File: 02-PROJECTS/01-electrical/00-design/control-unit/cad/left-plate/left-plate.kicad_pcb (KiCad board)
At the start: 2 copper layers, 100 x 56 mm, 22 parts, among them J1 plate cable header 2x6 shroud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, SW1 key - hatch, SW2 key - fuel door, U1 IS31FL3218-QFLS2-TR

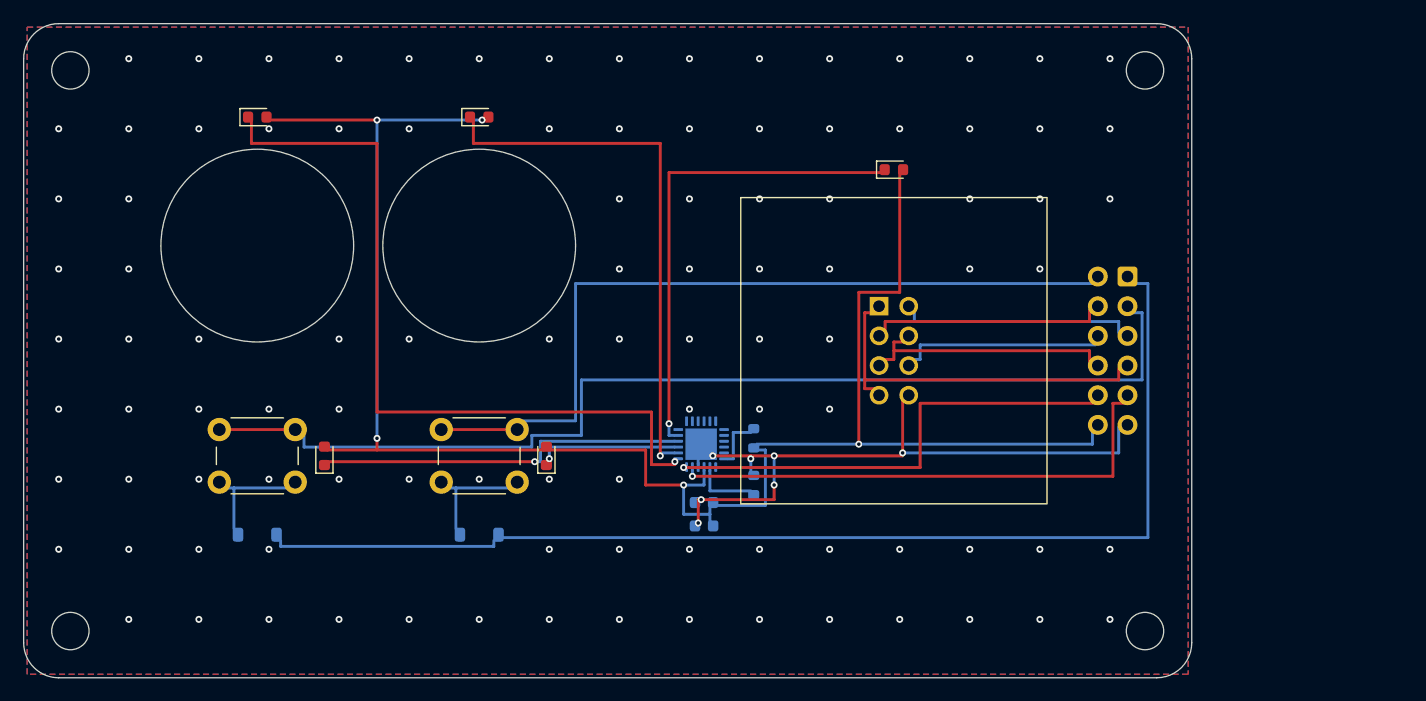
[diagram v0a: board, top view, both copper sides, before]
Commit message: Electrical: the left plate regenerated - P204 winks on the board at 19 mm, the wink lead on J2, the wink check in check.py (D-499, D-504)
Y22 done. ERC 0, DRC 0/0/0, check.py 29 checks 0 mismatches on the plate with check_winks (J2 against the L3-S1 rows that land on it, resistor values from cavity 11); the other boards unchanged. P204's footprint, J2's housing and run and R3/R4's part numbers confirm. The design README's plate row follows in the next commit with the export section.

Co-Authored-By: Claude Fable 5.1 <noreply@anthropic.com>
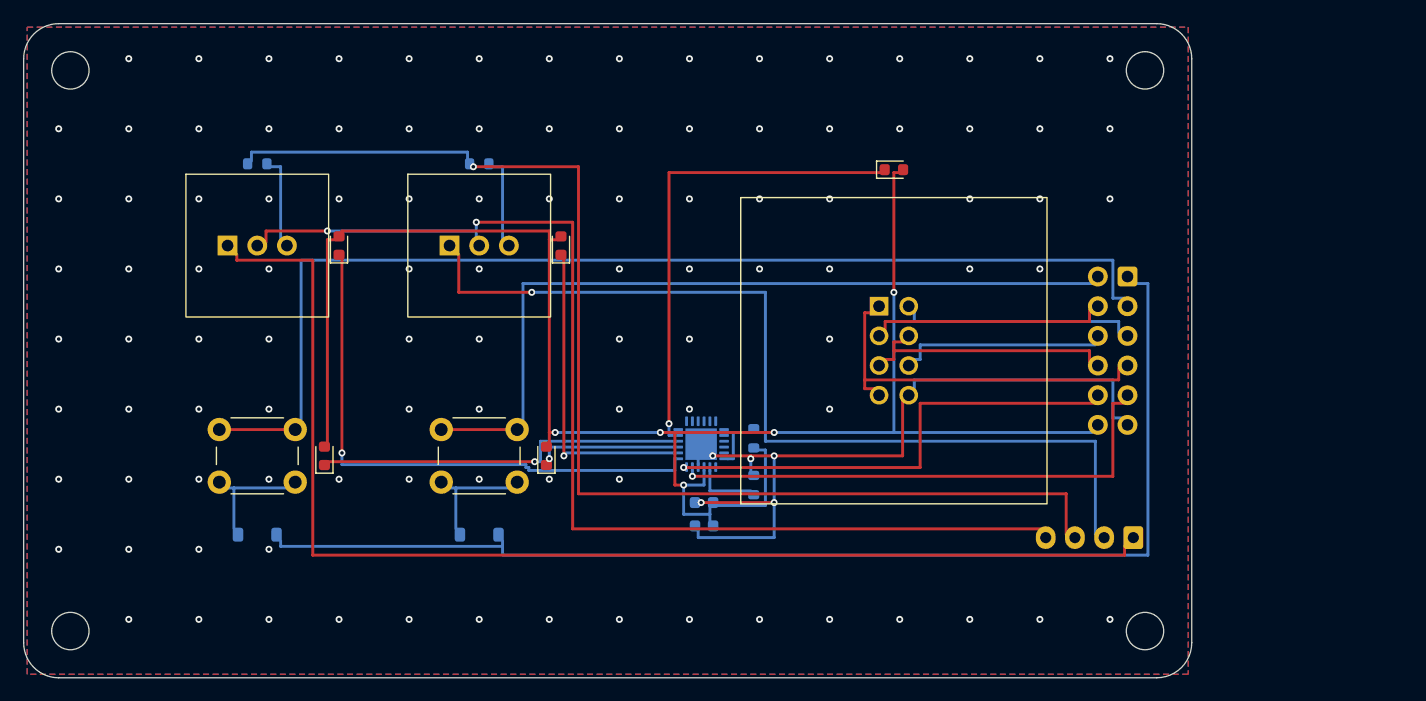
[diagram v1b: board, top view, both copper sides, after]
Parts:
- removed H5: wink L (P083) - clearance, no nets, left-plate:WinkSwitch_P083_Clearance_D16.5
- removed H6: wink R (P083) - clearance, no nets, left-plate:WinkSwitch_P083_Clearance_D16.5
- added J2: wink lead header 1x4 (L3-S1 9 / 10 / 11, commons), Connector_JST:JST_XH_B4B-XH-A_1x04_P2.50mm_Vertical, B.Cu at (95.0, 44.0)
- added R3: 18k, Resistor_SMD:R_0603_1608Metric, B.Cu at (20.0, 12.0)
- added R4: 33k, Resistor_SMD:R_0603_1608Metric, B.Cu at (39.0, 12.0)
- added SW3: wink - left (P204), left-plate:WinkSwitch_P204_SPDT_Placeholder, F.Cu at (20.0, 19.0)
- added SW4: wink - right (P204), left-plate:WinkSwitch_P204_SPDT_Placeholder, F.Cu at (39.0, 19.0)
- moved LED1 13.0 mm to (27.0, 19.0), turned to 90 degrees
- moved LED2 13.0 mm to (46.0, 19.0), turned to 90 degrees
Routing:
- net /WINK_L_NC: track 0.00 -> 102.5 mm
- net /WINK_REQ: track 0.00 -> 102.2 mm, vias 0 -> 1
- net /WINK_COM: track 0.00 -> 95.0 mm, vias 0 -> 2
- net /WINK_R_NC: track 0.00 -> 78.5 mm, vias 0 -> 1
- net /LED_WINK_R: track 46.2 -> 26.8 mm
- net /LED_WINK_L: track 66.2 -> 47.8 mm
- net GND: track 56.2 -> 65.5 mm
- net /WINK_R_NO: track 0.00 -> 7.25 mm
- net /WINK_L_NO: track 0.00 -> 7.25 mm
- net /+5V_PNL: track 155.2 -> 148.8 mm
- net /ROW1: track 97.2 -> 100.2 mm
- net /COL3: track 90.0 -> 92.5 mm
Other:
- board text added: "D-492 D-499 - provisional, confirm"
- board text added: "LEFT PLATE Y22 rev 0.02"
- board text removed: "D-492 - provisional, confirm"
- board text removed: "LEFT PLATE Y21 rev 0.01"

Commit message: Electrical: the CUR board takes the latching hazard button and the screen knob's header; its mock-up the knob (D-586, D-589, D-581)
Y62, Y50, Y51 (the CUR part). The plate board rev 0.03 from its generator: SW5 latching button with
R5 4.7 k and R6 47 k on a 5-way J2, LED6 the red triangle on OUT6 (the mirror symbol to OUT13, the
DCU's lights.h follows), J4 a STEMMA QT header for the knob's I2C board, the plate 118 x 56 (its
face's layout is block 01.60). ERC 0, DRC 0 with parity, check.py left-plate 31 / 0 with a new hazard
rule. The board script finishes leftovers with freerouting. The CUR mock-up's hazard opening and the
screen knob (24 / 24). The Digi-Key cart gains P219's board and lead.

Co-Authored-By: Claude Opus 5.5 <noreply@anthropic.com>
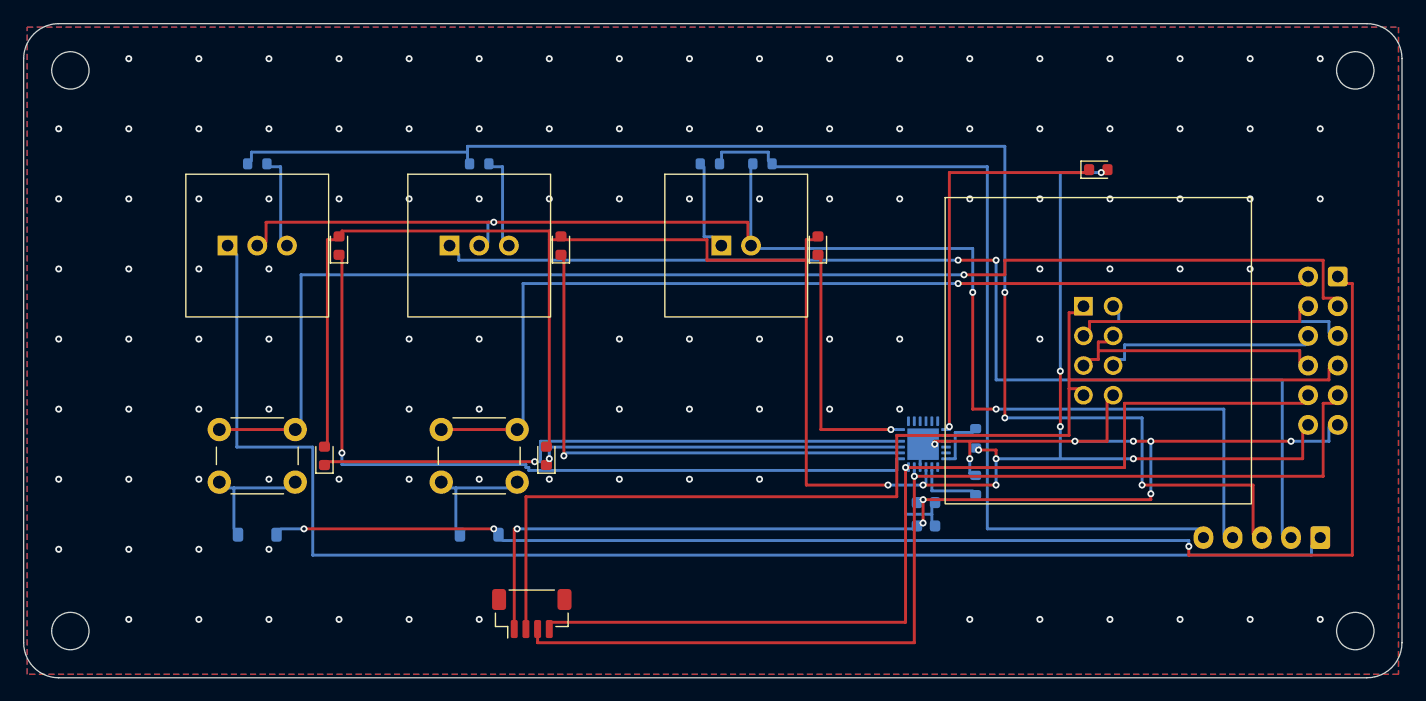
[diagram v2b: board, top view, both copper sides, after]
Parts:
- added J4: screen knob lead header (STEMMA QT, P219), Connector_JST:JST_SH_BM04B-SRSS-TB_1x04-1MP_P1.00mm_Vertical, F.Cu at (43.5, 50.5)
- added KN1: screen knob board (P219), left-plate:ScreenKnob_P219_Board_Placeholder, F.Cu at (61.0, 40.0)
- added LED6: LED 0603 - hazard red triangle (OUT6), LED_SMD:LED_0603_1608Metric, F.Cu at (68.0, 19.0)
- added R5: 4.7k, Resistor_SMD:R_0603_1608Metric, B.Cu at (58.8, 12.0)
- added R6: 47k, Resistor_SMD:R_0603_1608Metric, B.Cu at (63.2, 12.0)
- added SW5: hazard - latching (P226), left-plate:HazardSwitch_P226_Latching_Placeholder, F.Cu at (61.0, 19.0)
- J2: value wink lead header 1x4 (L3-S1 9 / 10 / 11, commons) -> wink lead header 1x5 (L3-S1 9 / 10 / 11, commons, L3-S1 6); footprint Connector_JST:JST_XH_B4B-XH-A_1x04_P2.50mm_Vertical -> Connector_JST:JST_XH_B5B-XH-A_1x05_P2.50mm_Vertical
- LED5: value LED 0603 - mirror stick symbol (OUT5) -> LED 0603 - mirror stick symbol (OUT13)
- moved C1 19.0 mm to (77.2, 43.0)
- moved C2 19.0 mm to (77.2, 41.0)
- moved R1 19.0 mm to (81.5, 39.5)
- moved R2 19.0 mm to (81.5, 35.5)
- moved U1 19.0 mm to (77.0, 36.0)
- moved H2 18.0 mm to (114.0, 4.00)
- moved H4 18.0 mm to (114.0, 52.0)
- moved J1 18.0 mm to (112.5, 21.6)
- moved JS1 17.5 mm to (92.0, 28.0)
- moved LED5 17.5 mm to (92.0, 12.5)
- moved J2 16.0 mm to (111.0, 44.0)
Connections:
- U1 pad 11: /LED_MIRROR -> unconnected-(U1-OUT5-Pad11)
- U1 pad 12: unconnected-(U1-OUT6-Pad12) -> /LED_HAZARD
- U1 pad 19: unconnected-(U1-OUT13-Pad19) -> /LED_MIRROR
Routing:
- net /HAZ_LADDER: track 0.00 -> 73.0 mm
- net +3V3: track 30.5 -> 97.5 mm
- net GND: track 65.5 -> 114.2 mm, vias 109 -> 124
- net /PNL_SDA: track 43.8 -> 89.8 mm
- net /PNL_SCL: track 41.0 -> 83.8 mm
- net /+5V_PNL: track 148.8 -> 184.8 mm, vias 5 -> 9
- net /WINK_COM: track 95.0 -> 116.8 mm, vias 2 -> 3
- net /LED_HAZARD: track 0.00 -> 21.2 mm, vias 0 -> 1
- net /LED_WINK_R: track 26.8 -> 45.8 mm
- net /LED_WINK_L: track 47.8 -> 66.8 mm
- net /LED_HATCH: track 12.0 -> 31.0 mm
- net /LED_FUEL: track 31.5 -> 50.5 mm
- net /WINK_REQ: track 102.2 -> 121.0 mm, vias 1 -> 3
- net /COL3: track 92.5 -> 110.5 mm, vias 0 -> 1
- net /COL2: track 65.5 -> 83.5 mm, vias 0 -> 1
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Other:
- board size 100 x 56 mm -> 118 x 56 mm
- board text added: "CUR PLATE Y62 rev 0.03"
- board text added: "D-492 D-499 D-586 D-589 - provisional, confirm"
- board text removed: "D-492 D-499 - provisional, confirm"
- board text removed: "LEFT PLATE Y22 rev 0.02"
